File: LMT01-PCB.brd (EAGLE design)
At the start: 127 x 30.5 mm, 29 parts, among them IC1 PIC18F47Q84, IC2 +12v, IC3 LM393D, IC4 MAX3467CPA, IC5 LM393D

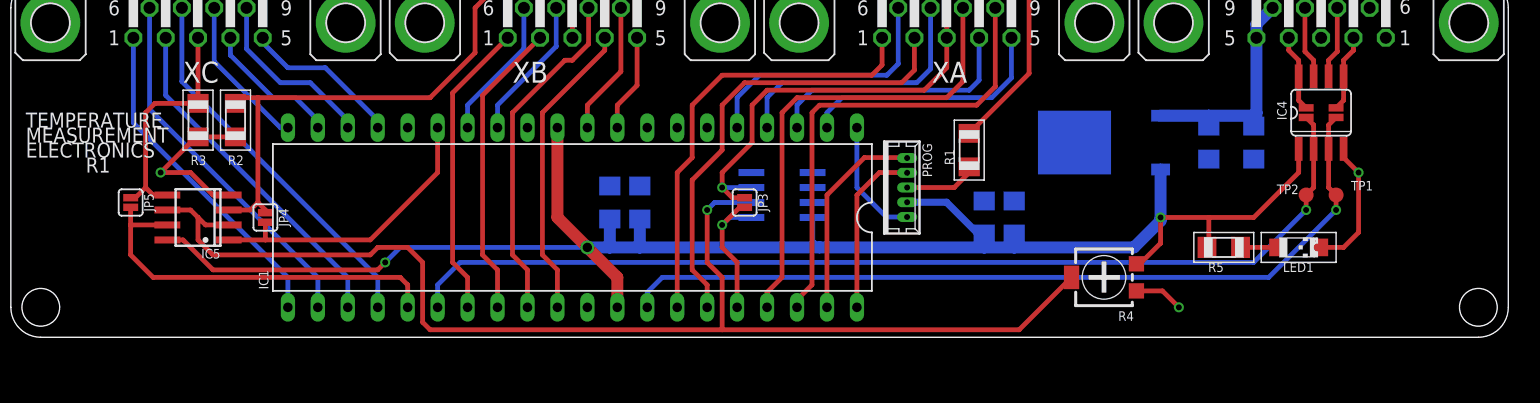
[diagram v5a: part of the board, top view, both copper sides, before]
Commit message: Adding test points
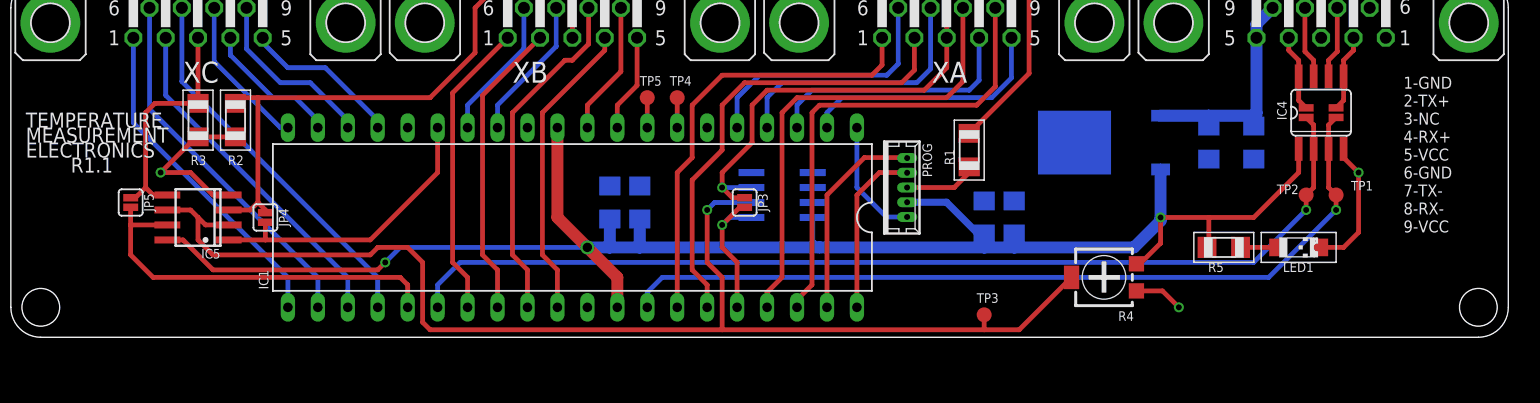
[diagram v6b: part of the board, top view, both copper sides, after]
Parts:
- added TP3, TP4, TP5: TPB1,27, testpad:B1,27
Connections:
- net N$21 renamed TX+
- net N$22 renamed TX-
- net N$23 renamed RX+
- net N$24 renamed RX-
- new net N$6: IC1.7, TP4.TP
- new net N$7: IC1.8, TP5.TP
- net N$4: now also TP3.TP
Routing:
- net N$7: track 0.00 -> 2.54 mm
- net N$6: track 0.00 -> 2.54 mm
- net N$4: track 104.9 -> 106.2 mm
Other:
- board text added: "1-GND 2-TX+ 3-NC 4-RX+ 5-VCC 6-GND 7-TX- 8-RX- 9-VCC"
- board text added: "R1.1"
- board text removed: "R1"
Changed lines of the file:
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@@
 <text x="1.27" y="16.51" size="1.27" layer="21" font="fixed">MEASUREMENT</text>
 <text x="1.27" y="15.24" size="1.27" layer="21" font="fixed">ELECTRONICS</text>
-<text x="6.35" y="13.97" size="1.27" layer="21" font="fixed">R1</text>
+<text x="5.08" y="13.97" size="1.27" layer="21" font="fixed">R1.1</text>
+<text x="118.11" y="8.89" size="1.016" layer="21" font="fixed">1-GND
+2-TX+
+3-NC
+4-RX+
+5-VCC
+6-GND
+7-TX-
+8-RX-
+9-VCC</text>
 </plain>
 <attributes>
@@
 <attribute name="VALUE" x="104.14" y="10.16" size="1.27" layer="27" rot="R180"/>
 </element>
+<element name="TP3" library="testpad" package="B1,27" value="TPB1,27" x="82.55" y="1.905" smashed="yes">
+<attribute name="TP_SIGNAL_NAME" value="" x="81.915" y="0" size="1" layer="37"/>
+<attribute name="NAME" x="81.915" y="2.921" size="0.8128" layer="25" font="fixed" ratio="10"/>
+</element>
+<element name="TP4" library="testpad" package="B1,27" value="TPB1,27" x="56.515" y="20.32" smashed="yes">
+<attribute name="TP_SIGNAL_NAME" value="" x="55.88" y="18.415" size="1" layer="37"/>
+<attribute name="NAME" x="55.88" y="21.336" size="0.8128" layer="25" font="fixed" ratio="10"/>
+</element>
+<element name="TP5" library="testpad" package="B1,27" value="TPB1,27" x="53.975" y="20.32" smashed="yes">
+<attribute name="TP_SIGNAL_NAME" value="" x="53.34" y="18.415" size="1" layer="37"/>
+<attribute name="NAME" x="53.34" y="21.336" size="0.8128" layer="25" font="fixed" ratio="10"/>
+</element>
 </elements>
 <signals>
@@
 <wire x1="53.975" y1="3.81" x2="53.975" y2="2.54" width="0.4064" layer="16"/>
 </signal>
-<signal name="N$21">
+<signal name="TX+">
 <contactref element="IC4" pad="5"/>
 <contactref element="X2" pad="2"/>
@@
 <wire x1="113.03" y1="20.0914" x2="112.395" y2="19.4564" width="0.4064" layer="1"/>
 </signal>
-<signal name="N$22">
+<signal name="TX-">
 <contactref element="IC4" pad="6"/>
 <contactref element="X2" pad="7"/>
@@
 <wire x1="111.76" y1="23.495" x2="111.76" y2="22.1234" width="0.4064" layer="1"/>
 </signal>
-<signal name="N$23">
+<signal name="RX+">
 <contactref element="IC4" pad="8"/>
 <contactref element="X2" pad="4"/>
@@
 <wire x1="109.22" y1="20.0914" x2="109.855" y2="19.4564" width="0.4064" layer="1"/>
 </signal>
-<signal name="N$24">
+<signal name="RX-">
 <contactref element="IC4" pad="7"/>
 <contactref element="X2" pad="8"/>
@@
 <wire x1="15.875" y1="10.16" x2="15.24" y2="10.795" width="0.4064" layer="1"/>
 <wire x1="15.24" y1="10.795" x2="13.275" y2="10.795" width="0.4064" layer="1"/>
-<wire x1="60.325" y1="0.635" x2="85.515" y2="0.635" width="0.4064" layer="1"/>
+<wire x1="60.325" y1="0.635" x2="82.55" y2="0.635" width="0.4064" layer="1"/>
+<wire x1="82.55" y1="0.635" x2="85.515" y2="0.635" width="0.4064" layer="1"/>
 <wire x1="85.515" y1="0.635" x2="89.96" y2="5.08" width="0.4064" layer="1"/>
 <wire x1="62.805" y1="11.43" x2="59.69" y2="11.43" width="0.4064" layer="16"/>
@@
 <wire x1="34.925" y1="1.27" x2="35.56" y2="0.635" width="0.4064" layer="1"/>
 <wire x1="35.56" y1="0.635" x2="60.325" y2="0.635" width="0.4064" layer="1"/>
+<contactref element="TP3" pad="TP"/>
+<wire x1="82.55" y1="1.905" x2="82.55" y2="0.635" width="0.4064" layer="1"/>
 </signal>
 <signal name="COMMONA_BUF">
@@
 <wire x1="104.292" y1="7.62" x2="107.47" y2="7.62" width="0.4064" layer="1"/>
 </signal>
+<signal name="N$6">
+<contactref element="IC1" pad="7"/>
+<contactref element="TP4" pad="TP"/>
+<wire x1="56.515" y1="17.78" x2="56.515" y2="20.32" width="0.4064" layer="1"/>
+</signal>
+<signal name="N$7">
+<contactref element="IC1" pad="8"/>
+<contactref element="TP5" pad="TP"/>
+<wire x1="53.975" y1="17.78" x2="53.975" y2="20.32" width="0.4064" layer="1"/>
+</signal>
 </signals>
 <errors>
@@
 </board>
 </drawing>
+<compatibility>
+<note version="6.3" minversion="6.2.2" severity="warning">
+Since Version 6.2.2 text objects can contain more than one line,
+which will not be processed correctly with this version.
+</note>
+</compatibility>
 </eagle>

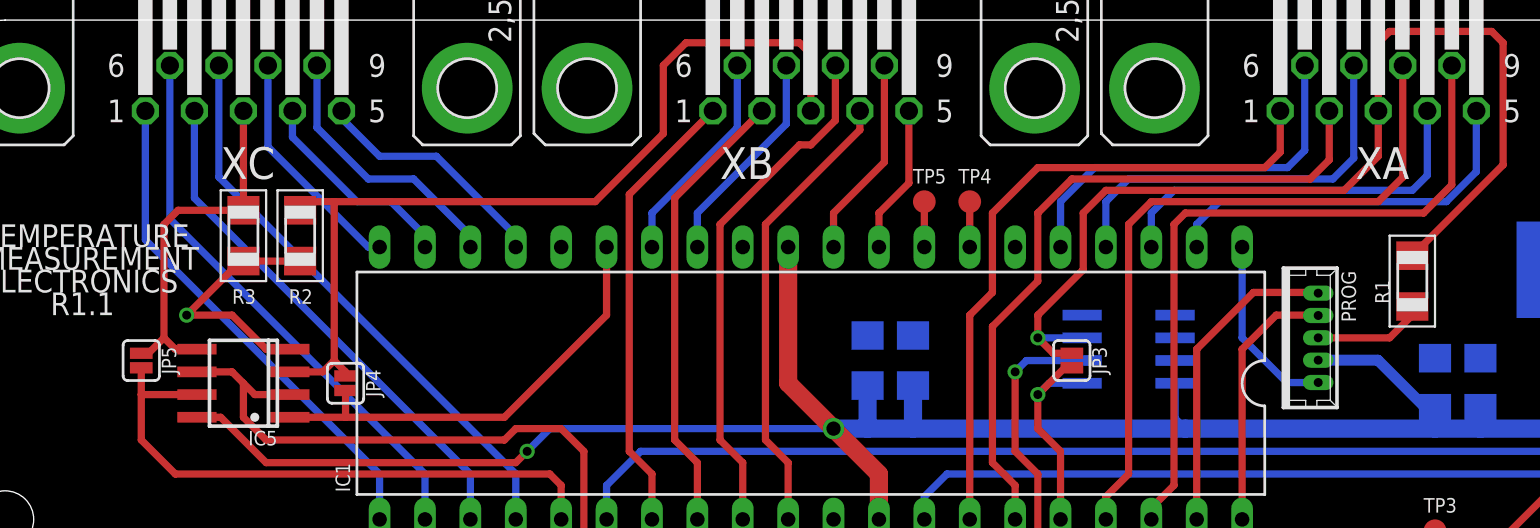
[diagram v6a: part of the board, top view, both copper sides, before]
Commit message: Adding more test points and deleting jumpers
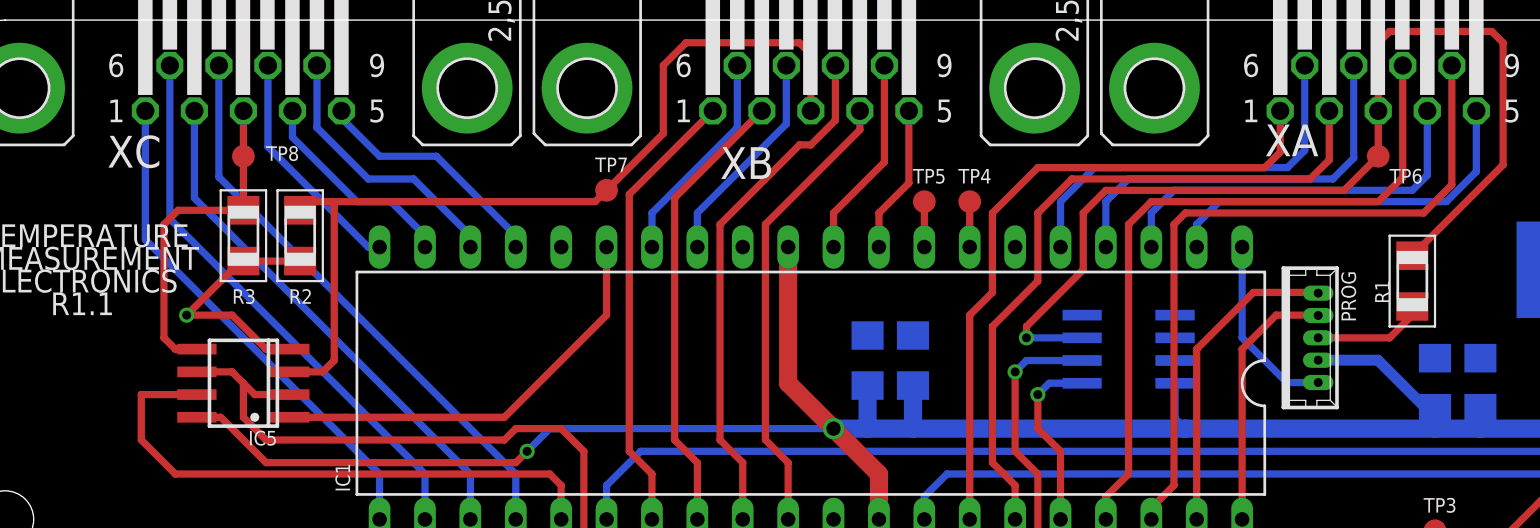
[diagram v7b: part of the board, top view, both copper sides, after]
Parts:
- removed JP3, JP4, JP5: JUMPER-SMT_2_NO_SILK, SparkFun-Jumpers:SMT-JUMPER_2_NO_SILK
- added TP6, TP7, TP8: TPB1,27, testpad:B1,27
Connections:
- net COMMONA: now also TP6.TP; no longer JP3.1
- net COMMONA_BUF: no longer JP3.2
- net COMMONB: now also TP7.TP; no longer JP4.1
- net COMMONB_BUF: no longer JP4.2
- net COMMONC: now also TP8.TP; no longer JP5.1
- net COMMONC_BUF: no longer JP5.2
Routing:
- net COMMONA_BUF: track 12.8 -> 10.3 mm
- net COMMONC: track 20.4 -> 18.8 mm
- net COMMONB_BUF: track 25.4 -> 23.9 mm
- net COMMONC_BUF: track 33.6 -> 32.1 mm
- net COMMONA: track 58.5 -> 57.1 mm
- net COMMONB: track 50.9 -> 49.8 mm
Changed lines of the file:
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@@
 <attribute name="OC_NEWARK" value="unknown" x="79.375" y="26.67" size="1.778" layer="27" display="off"/>
 <attribute name="MPN" value="" x="79.375" y="26.67" size="1.778" layer="27" display="off"/>
-<attribute name="NAME" x="78.105" y="21.59" size="1.778" layer="25" font="fixed" ratio="10"/>
+<attribute name="NAME" x="73.025" y="22.86" size="1.778" layer="25" font="fixed" ratio="10"/>
 <attribute name="VALUE" x="74.295" y="40.64" size="1.778" layer="27" ratio="10"/>
 </element>
@@
 <attribute name="OC_NEWARK" value="unknown" x="15.875" y="26.67" size="1.778" layer="27" display="off"/>
 <attribute name="MPN" value="" x="15.875" y="26.67" size="1.778" layer="27" display="off"/>
-<attribute name="NAME" x="14.605" y="21.59" size="1.778" layer="25" font="fixed" ratio="10"/>
+<attribute name="NAME" x="8.255" y="22.225" size="1.778" layer="25" font="fixed" ratio="10"/>
 <attribute name="VALUE" x="10.795" y="40.64" size="1.778" layer="27" ratio="10"/>
 </element>
@@
 <attribute name="VALUE" x="95.25" y="9.125" size="1.27" layer="27" rot="R180"/>
 </element>
-<element name="JP3" library="SparkFun-Jumpers" package="SMT-JUMPER_2_NO_SILK" value="JUMPER-SMT_2_NO_SILK" x="62.23" y="11.43" smashed="yes" rot="R270">
-<attribute name="NAME" x="63.373" y="11.43" size="0.8128" layer="25" font="fixed" ratio="20" rot="R270" align="bottom-center"/>
-</element>
-<element name="JP4" library="SparkFun-Jumpers" package="SMT-JUMPER_2_NO_SILK" value="JUMPER-SMT_2_NO_SILK" x="21.59" y="10.16" smashed="yes" rot="R270">
-<attribute name="NAME" x="22.733" y="10.16" size="0.8128" layer="25" font="fixed" ratio="20" rot="R270" align="bottom-center"/>
-</element>
-<element name="JP5" library="SparkFun-Jumpers" package="SMT-JUMPER_2_NO_SILK" value="JUMPER-SMT_2_NO_SILK" x="10.16" y="11.43" smashed="yes" rot="R270">
-<attribute name="NAME" x="11.303" y="11.43" size="0.8128" layer="25" font="fixed" ratio="20" rot="R270" align="bottom-center"/>
-</element>
 <element name="LED1" library="led" package="CHIPLED_1206" value="" x="109.22" y="7.62" smashed="yes" rot="R270">
 <attribute name="NAME" x="110.49" y="6.35" size="0.8128" layer="25" font="fixed" rot="R180"/>
@@
 <attribute name="TP_SIGNAL_NAME" value="" x="53.34" y="18.415" size="1" layer="37"/>
 <attribute name="NAME" x="53.34" y="21.336" size="0.8128" layer="25" font="fixed" ratio="10"/>
+</element>
+<element name="TP6" library="testpad" package="B1,27" value="TPB1,27" x="79.375" y="22.86" smashed="yes">
+<attribute name="TP_SIGNAL_NAME" value="" x="78.74" y="20.955" size="1" layer="37"/>
+<attribute name="NAME" x="80.01" y="21.336" size="0.8128" layer="25" font="fixed" ratio="10"/>
+<attribute name="VALUE" x="78.74" y="22.098" size="0.0254" layer="27"/>
+</element>
+<element name="TP7" library="testpad" package="B1,27" value="TPB1,27" x="36.195" y="20.955" smashed="yes">
+<attribute name="TP_SIGNAL_NAME" value="" x="35.56" y="19.05" size="1" layer="37"/>
+<attribute name="NAME" x="35.56" y="21.971" size="0.8128" layer="25" font="fixed" ratio="10"/>
+<attribute name="VALUE" x="35.56" y="20.193" size="0.0254" layer="27"/>
+</element>
+<element name="TP8" library="testpad" package="B1,27" value="TPB1,27" x="15.875" y="22.86" smashed="yes">
+<attribute name="TP_SIGNAL_NAME" value="" x="15.24" y="20.955" size="1" layer="37"/>
+<attribute name="NAME" x="17.145" y="22.606" size="0.8128" layer="25" font="fixed" ratio="10"/>
+<attribute name="VALUE" x="15.24" y="22.098" size="0.0254" layer="27"/>
 </element>
 </elements>
@@
 <contactref element="IC3" pad="3"/>
 <wire x1="62.865" y1="19.685" x2="62.865" y2="16.51" width="0.4064" layer="1"/>
-<wire x1="62.865" y1="16.51" x2="60.325" y2="13.97" width="0.4064" layer="1"/>
-<wire x1="60.325" y1="13.97" x2="60.325" y2="12.7" width="0.4064" layer="1"/>
-<via x="60.325" y="12.7" extent="1-16" drill="0.5"/>
-<wire x1="60.325" y1="12.7" x2="62.805" y2="12.7" width="0.4064" layer="16"/>
+<wire x1="62.865" y1="16.51" x2="59.69" y2="13.335" width="0.4064" layer="1"/>
+<wire x1="59.69" y1="13.335" x2="59.69" y2="12.7" width="0.4064" layer="1"/>
+<via x="59.69" y="12.7" extent="1-16" drill="0.5"/>
 <wire x1="79.375" y1="25.4" x2="79.375" y2="22.86" width="0.4064" layer="1"/>
-<contactref element="JP3" pad="1"/>
-<wire x1="62.23" y1="11.8364" x2="61.1886" y2="11.8364" width="0.4064" layer="1"/>
-<wire x1="61.1886" y1="11.8364" x2="60.325" y2="12.7" width="0.4064" layer="1"/>
+<wire x1="62.805" y1="12.7" x2="59.69" y2="12.7" width="0.4064" layer="16"/>
+<contactref element="TP6" pad="TP"/>
 </signal>
 <signal name="COMMONB">
 <contactref element="XB" pad="3"/>
 <contactref element="R2" pad="2"/>
-<wire x1="35.56" y1="20.32" x2="39.37" y2="24.13" width="0.4064" layer="1"/>
+<wire x1="36.195" y1="20.955" x2="39.37" y2="24.13" width="0.4064" layer="1"/>
 <wire x1="39.37" y1="24.13" x2="39.37" y2="27.94" width="0.4064" layer="1"/>
 <wire x1="39.37" y1="27.94" x2="40.64" y2="29.21" width="0.4064" layer="1"/>
@@
 <wire x1="20.32" y1="10.795" x2="20.955" y2="11.43" width="0.4064" layer="1"/>
 <wire x1="20.955" y1="11.43" x2="20.955" y2="20.32" width="0.4064" layer="1"/>
-<contactref element="JP4" pad="1"/>
-<wire x1="21.59" y1="10.5664" x2="21.59" y2="10.795" width="0.4064" layer="1"/>
-<wire x1="21.59" y1="10.795" x2="20.955" y2="11.43" width="0.4064" layer="1"/>
+<contactref element="TP7" pad="TP"/>
+<wire x1="36.195" y1="20.955" x2="35.56" y2="20.32" width="0.4064" layer="1"/>
 </signal>
 <signal name="COMMONC">
 <contactref element="XC" pad="3"/>
 <contactref element="R3" pad="2"/>
-<wire x1="15.875" y1="25.4" x2="15.875" y2="19.837" width="0.4064" layer="1"/>
 <contactref element="IC5" pad="5"/>
+<wire x1="15.875" y1="22.86" x2="15.875" y2="19.837" width="0.4064" layer="1"/>
 <wire x1="15.875" y1="19.837" x2="12.217" y2="19.837" width="0.4064" layer="1"/>
 <wire x1="12.217" y1="19.837" x2="11.43" y2="19.05" width="0.4064" layer="1"/>
@@
 <wire x1="11.43" y1="12.7" x2="12.065" y2="12.065" width="0.4064" layer="1"/>
 <wire x1="12.065" y1="12.065" x2="13.275" y2="12.065" width="0.4064" layer="1"/>
-<contactref element="JP5" pad="1"/>
-<wire x1="10.16" y1="11.8364" x2="10.5664" y2="11.8364" width="0.4064" layer="1"/>
-<wire x1="10.5664" y1="11.8364" x2="11.43" y2="12.7" width="0.4064" layer="1"/>
+<contactref element="TP8" pad="TP"/>
+<wire x1="15.875" y1="25.4" x2="15.875" y2="22.86" width="0.4064" layer="1"/>
 </signal>
 <signal name="N$1">
@@
 <wire x1="60.325" y1="9.525" x2="60.96" y2="10.16" width="0.4064" layer="16"/>
 <wire x1="60.96" y1="10.16" x2="62.805" y2="10.16" width="0.4064" layer="16"/>
-<contactref element="JP3" pad="2"/>
-<wire x1="62.23" y1="11.0236" x2="61.8236" y2="11.0236" width="0.4064" layer="1"/>
-<wire x1="61.8236" y1="11.0236" x2="60.325" y2="9.525" width="0.4064" layer="1"/>
 </signal>
 <signal name="COMMONB_BUF">
@@
 <wire x1="30.48" y1="8.255" x2="36.195" y2="13.97" width="0.4064" layer="1"/>
 <wire x1="36.195" y1="13.97" x2="36.195" y2="17.78" width="0.4064" layer="1"/>
-<contactref element="JP4" pad="2"/>
-<wire x1="21.59" y1="9.7536" x2="21.59" y2="8.255" width="0.4064" layer="1"/>
 </signal>
 <signal name="COMMONC_BUF">
@@
 <wire x1="10.16" y1="9.525" x2="10.16" y2="6.985" width="0.4064" layer="1"/>
 <wire x1="10.16" y1="6.985" x2="12.065" y2="5.08" width="0.4064" layer="1"/>
-<contactref element="JP5" pad="2"/>
-<wire x1="10.16" y1="9.525" x2="10.16" y2="11.0236" width="0.4064" layer="1"/>
 </signal>
 <signal name="N$5">

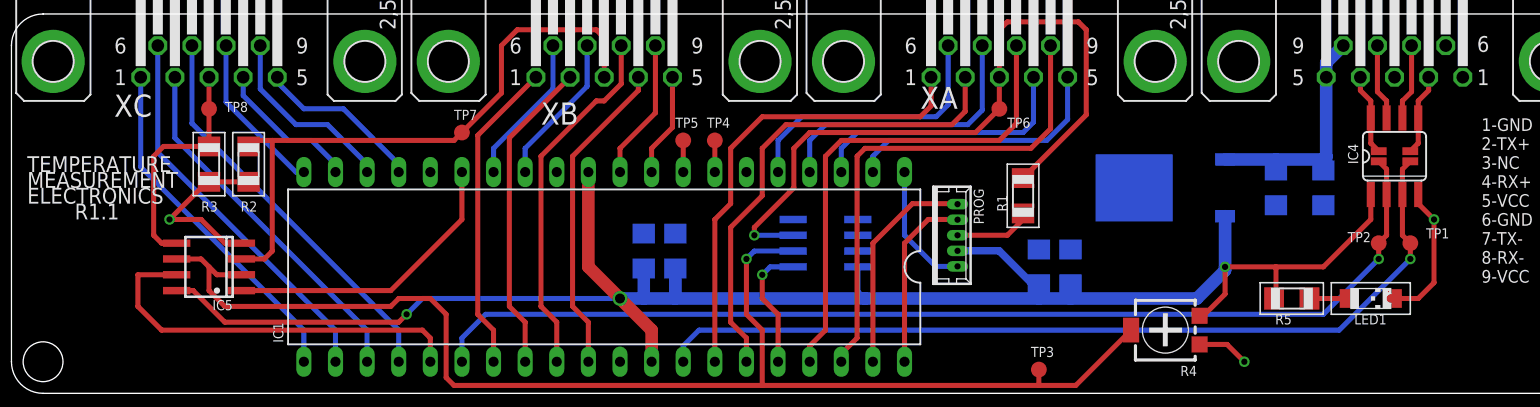
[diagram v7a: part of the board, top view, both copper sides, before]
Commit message: Adding RS-485 capability
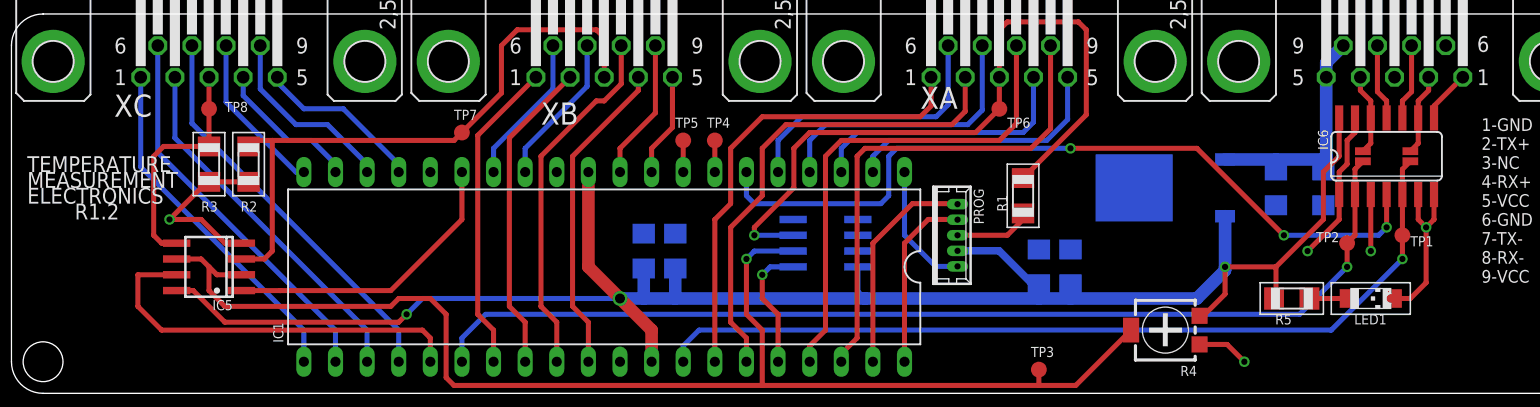
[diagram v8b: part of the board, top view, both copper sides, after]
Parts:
- removed IC4: MAX3467CPA, maxim:SO08
- added IC6: MAX3465CSD, maxim:SO14
- moved TP2 2.54 mm to (107.3, 12.1)
- moved JP1 1.27 mm to (108.6, 19.1)
- moved TP1 0.90 mm to (111.8, 12.7)
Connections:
- new net N$9: IC1.6, IC6.4
- net +5V: now also IC6.14; no longer IC4.1
- net GND: now also IC6.1, IC6.13, IC6.3, IC6.6, IC6.7, IC6.8; no longer IC4.4
- net RX+: now also IC6.12; no longer IC4.8
- net RX-: now also IC6.11; no longer IC4.7
- net TX+: now also IC6.9; no longer IC4.5
- net TX-: now also IC6.10; no longer IC4.6
- net UARTRX: now also IC6.2; no longer IC4.2
- net UARTTX: now also IC6.5; no longer IC4.3
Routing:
- net N$9: track 0.00 -> 63.1 mm, vias 0 -> 3
- net GND: track 36.1 -> 59.1 mm, vias 3 -> 5
- net +5V: track 149.2 -> 152.0 mm
- net UARTRX: track 86.6 -> 84.4 mm
- net UARTTX: track 71.0 -> 70.1 mm
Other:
- board text added: "R1.2"
- board text removed: "R1.1"
